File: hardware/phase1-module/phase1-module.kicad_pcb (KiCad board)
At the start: 4 copper layers, 100 x 80 mm, 144 parts, among them J1 VBUS IN, J2 SWD, J3 UART, J4 OUTPUT, J5 BACKPLANE, J6 FAN, Q1 CSD18563Q5A, Q2 CSD18563Q5A, Q3 60V NFET, Q4 60V NFET, Q5 2N7002, Q6 2N7002, Q7 2N7002, Q8 2N7002, Q9 2N7002, U1 DAC80502DRXT, U10 STM32G431CBT6, U11 TCAN1042HGV, U2 OPA2333, U3 LM5145RGYR, U4 INA240A3, U5 INA228, U6 LTC7004, U7 TLV7011DCK, U8 LMR36015AQRNXRQ1, U9 NCP1117-3.3, Y1 8MHz

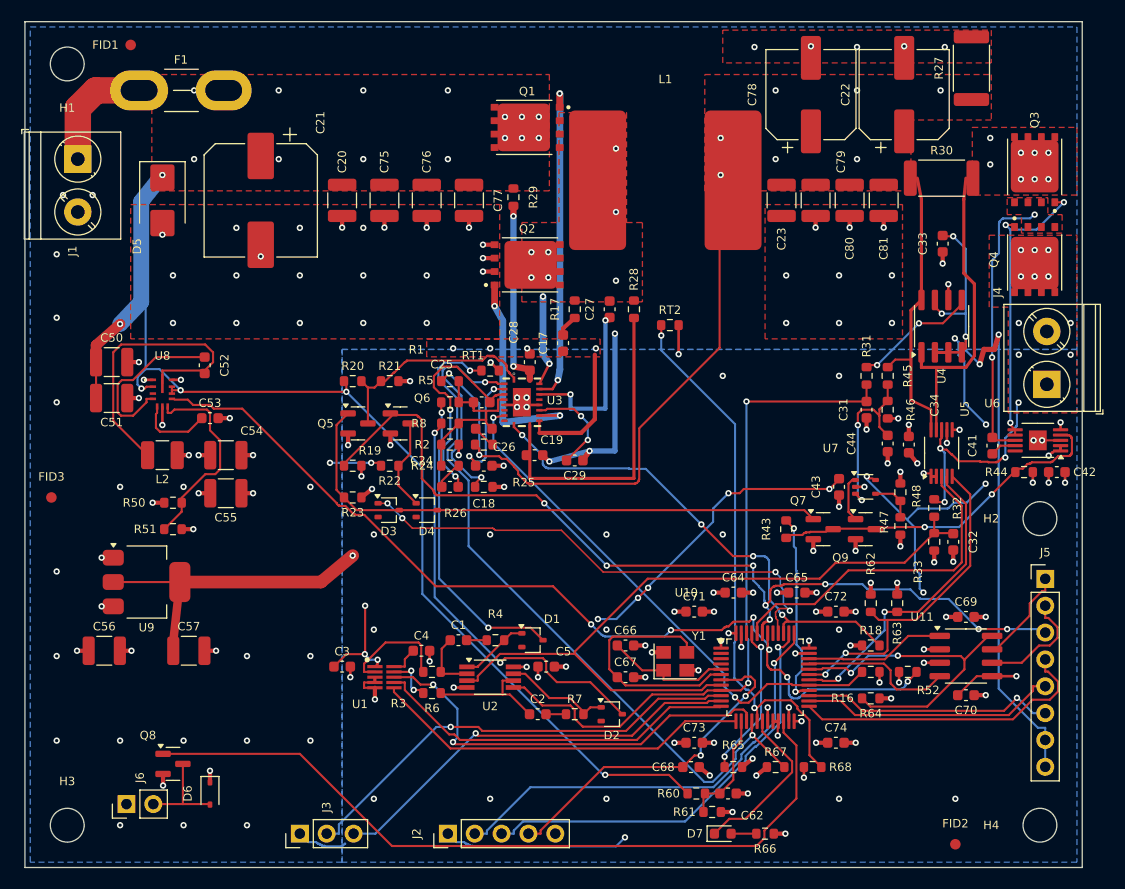
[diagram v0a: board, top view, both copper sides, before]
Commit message: Phase-1 board: route OVP_TRIP to MCU PB4 so the OVP trip can latch
The TLV7011 output only reached Q9 (disconnect), so an overvoltage
opened the output but left the LM5145 running and nothing latched.
OVP_TRIP now also goes to U10 pin 41 (PB4, a spare pin), where the
firmware 0.2 EXTI handler kills EN and latches OVP_HW.

Schematic: surgical edits (OVP_TRIP local labels -> global, PB4
no-connect -> OVP_TRIP label); gen_phase1.py / sheets_common.py
mirror it (ovp_to_mcu param, EXPECTED_NETS). check_netlist and
check_footprints pass.

Board: 21 signal nets in the U10-U7 region ripped and re-routed with
Freerouting 1.9 + finish_routes, fb_reroute rerun, three overlap stubs
trimmed. DRC: 0 unconnected, 0 errors, 10 silk warnings (was 11).
Fab zip regenerated; placement and BOM unchanged.

Co-Authored-By: Claude Opus 5.5 (1M context) <noreply@anthropic.com>
Claude-Session: https://claude.ai/code/session_01NmR2rbcK8CFj3PgzqsaRtW
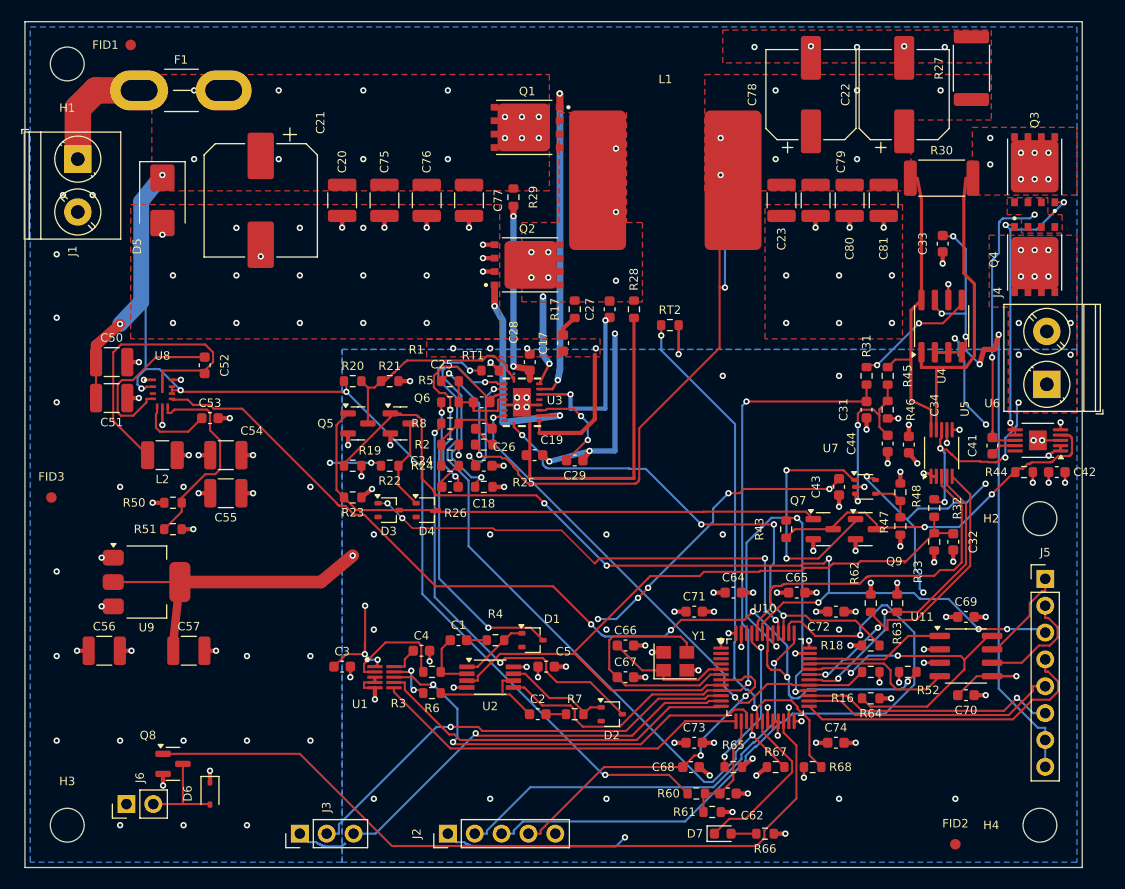
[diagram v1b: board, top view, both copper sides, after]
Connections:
- U10 pad 41: unconnected-(U10-PB4-Pad41) -> OVP_TRIP
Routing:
- net OVP_TRIP: track 4.43 -> 40.6 mm, vias 0 -> 3
- net SWCLK: track 40.4 -> 66.3 mm
- net VOUT_INT: track 80.3 -> 91.8 mm, vias 9 -> 10
- net HW_EN: track 84.4 -> 92.0 mm, vias 8 -> 6
- net DISC_INP: track 27.9 -> 34.7 mm
- net AUX_PG: track 88.0 -> 93.5 mm, vias 6 -> 5
- net PS_PGOOD: track 47.3 -> 50.3 mm
- net 3V3: track 84.7 -> 87.6 mm
- net OUT_REQ: track 17.3 -> 19.4 mm
- net 5V0: track 82.2 -> 83.8 mm
- net AGND: track 99.5 -> 101.0 mm
- net I2C_SCL: track 32.4 -> 30.9 mm
- net PS_EN: track 20.0 -> 21.2 mm
- net DISC_SRC: track 25.9 -> 26.8 mm
- net PS_COMP: track 20.5 -> 21.3 mm
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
